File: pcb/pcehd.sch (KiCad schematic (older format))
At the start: 3 parts, among them U1 AP7361

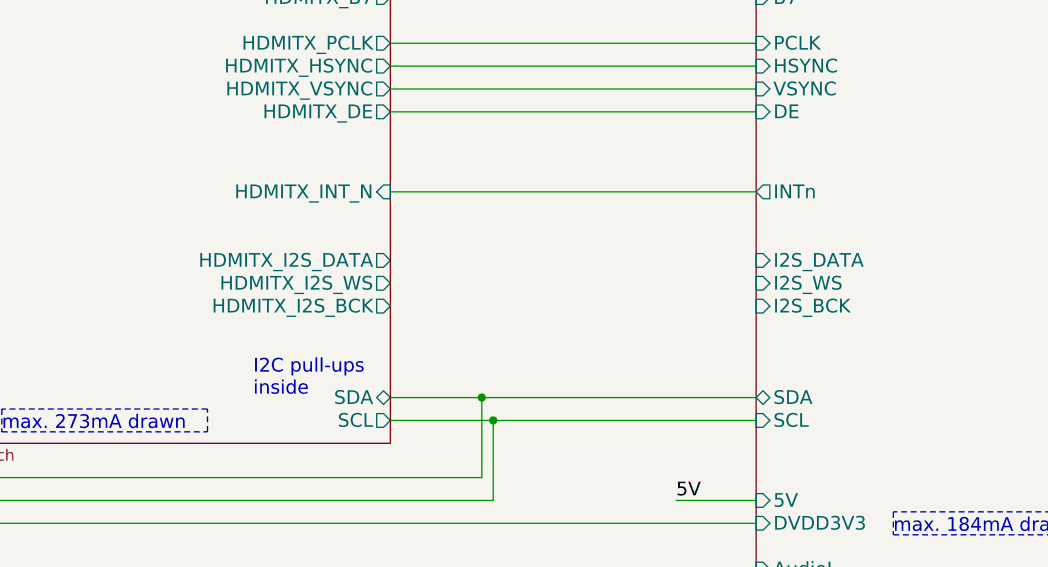
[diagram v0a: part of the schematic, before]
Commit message: Finished initial schematic with audio
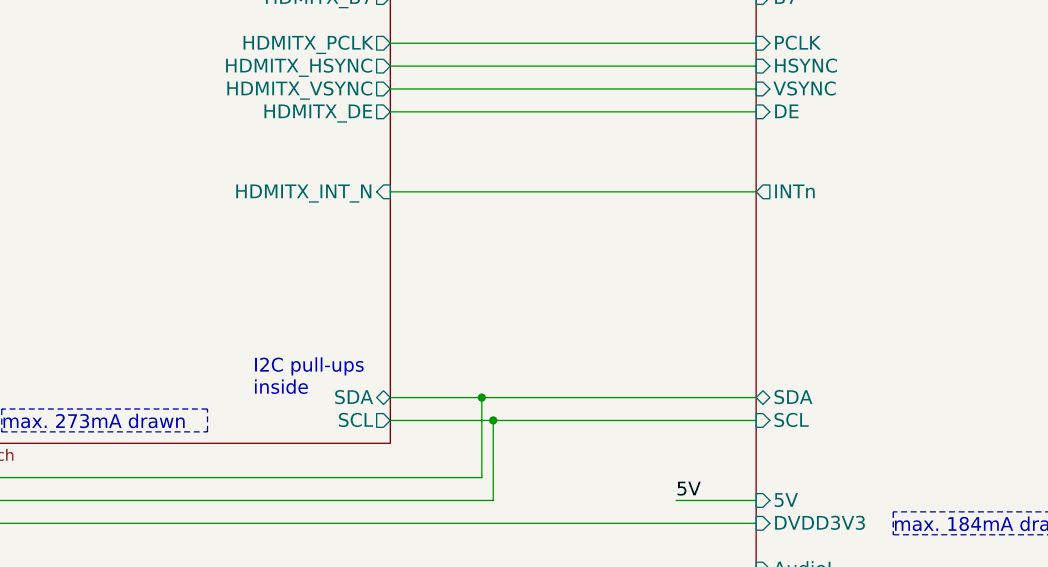
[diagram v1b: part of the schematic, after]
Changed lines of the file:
@@
 EESchema Schematic File Version 4
+LIBS:pcehd-cache
 EELAYER 30 0
 EELAYER END
@@
 F55 "DCK" I L 4650 4200 60
 F56 "CEK" I L 4650 4100 60
-F57 "HDMITX_I2S_DATA" O R 6750 4950 60
-F58 "HDMITX_I2S_WS" O R 6750 5050 60
-F59 "HDMITX_I2S_BCK" O R 6750 5150 60
-F60 "VD1" I L 4650 4750 60
-F61 "VD0" I L 4650 4650 60
-F62 "VD2" I L 4650 4850 60
-F63 "DDIR" O L 4650 2050 60
-F64 "A8" I L 4650 3000 60
-F65 "A9" I L 4650 3100 60
-F66 "A10" I L 4650 3200 60
-F67 "A11" I L 4650 3300 60
-F68 "A12" I L 4650 3400 60
-F69 "A16" I L 4650 3500 60
-F70 "A20" I L 4650 3600 60
-F71 "DCKSI" I L 4650 4300 60
-F72 "CDD" O L 4650 4400 60
-F73 "RST_N" O L 4650 4500 60
-F74 "SPBG" I L 4650 5450 60
-F75 "VD5" I L 4650 5150 60
-F76 "VD6" I L 4650 5250 60
-F77 "VD7" I L 4650 5350 60
+F57 "VD1" I L 4650 4750 60
+F58 "VD0" I L 4650 4650 60
+F59 "VD2" I L 4650 4850 60
+F60 "DDIR" O L 4650 2050 60
+F61 "A8" I L 4650 3000 60
+F62 "A9" I L 4650 3100 60
+F63 "A10" I L 4650 3200 60
+F64 "A11" I L 4650 3300 60
+F65 "A12" I L 4650 3400 60
+F66 "A16" I L 4650 3500 60
+F67 "A20" I L 4650 3600 60
+F68 "DCKSI" I L 4650 4300 60
+F69 "CDD" O L 4650 4400 60
+F70 "RST_N" O L 4650 4500 60
+F71 "SPBG" I L 4650 5450 60
+F72 "VD5" I L 4650 5150 60
+F73 "VD6" I L 4650 5250 60
+F74 "VD7" I L 4650 5350 60
 $EndSheet
 Wire Wire Line
@@
 F33 "DVDD3V3" I L 8350 6100 60
 F34 "5V" I L 8350 6000 60
-F35 "I2S_DATA" I L 8350 4950 60
-F36 "I2S_WS" I L 8350 5050 60
-F37 "I2S_BCK" I L 8350 5150 60
-F38 "AudioL" I L 8350 6300 60
-F39 "AudioR" I L 8350 6400 60
+F35 "AudioL" I L 8350 6300 60
+F36 "AudioR" I L 8350 6400 60
 $EndSheet
 $Sheet

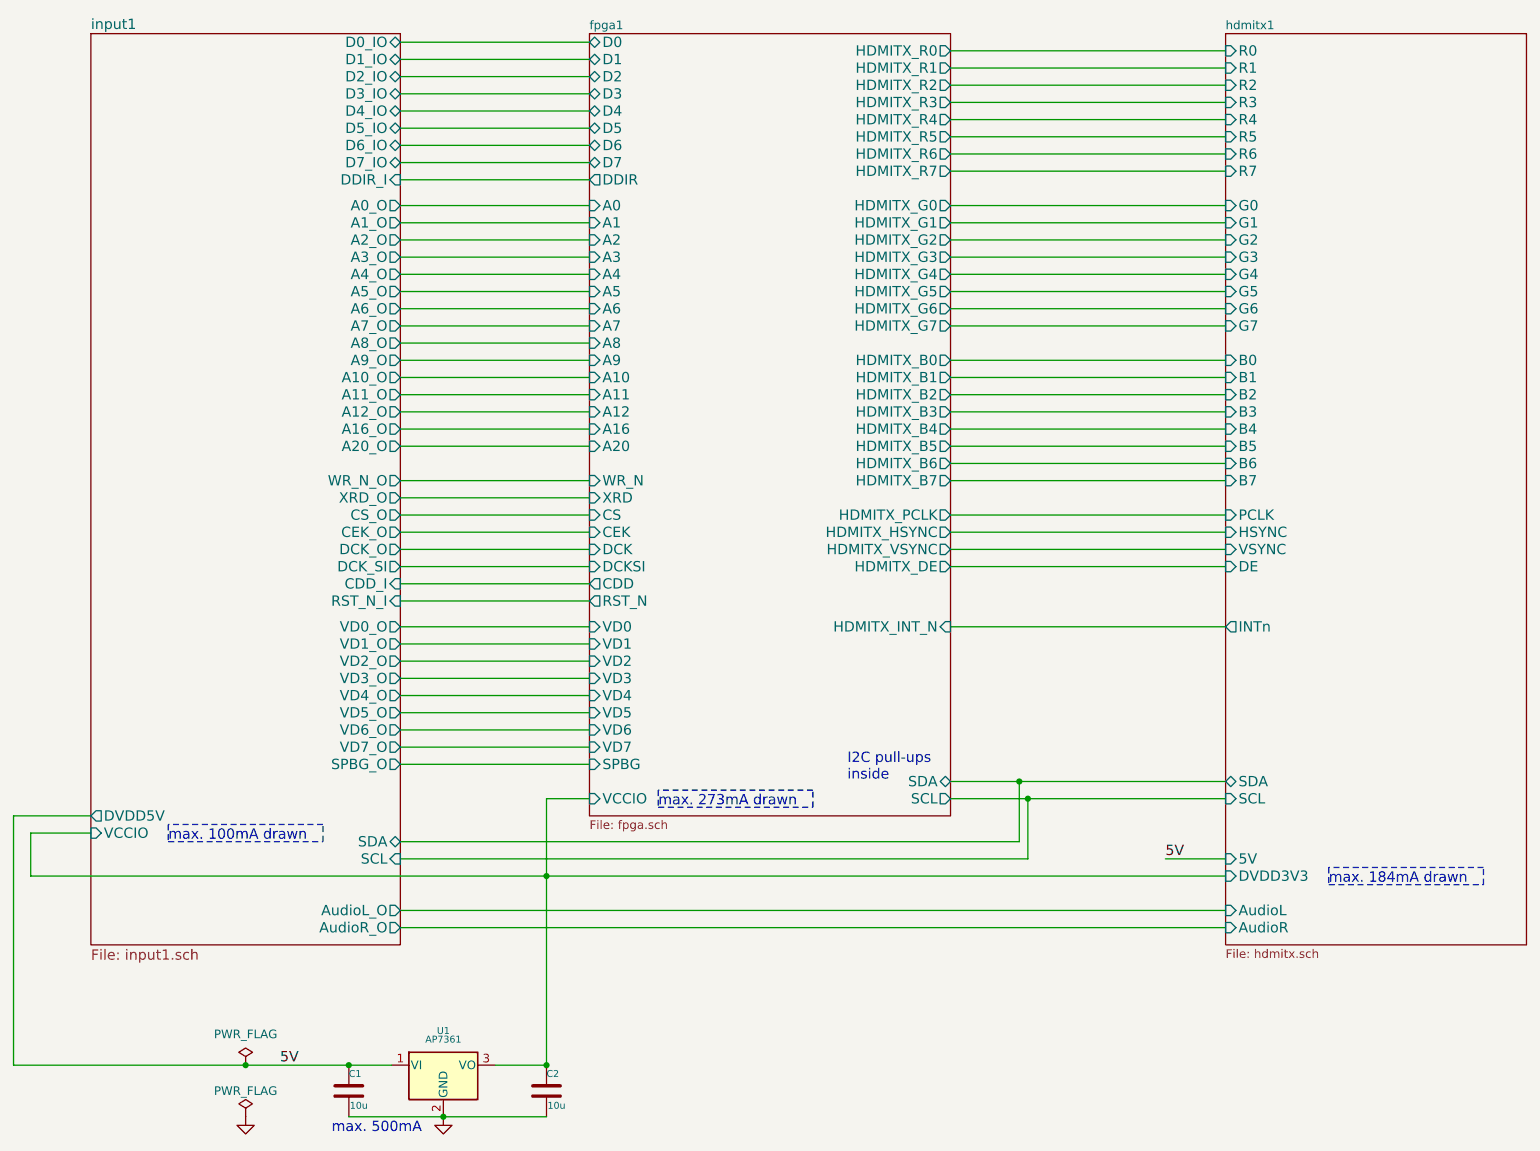
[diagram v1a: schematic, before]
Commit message: Cleaned up schematic, moved connections to busses
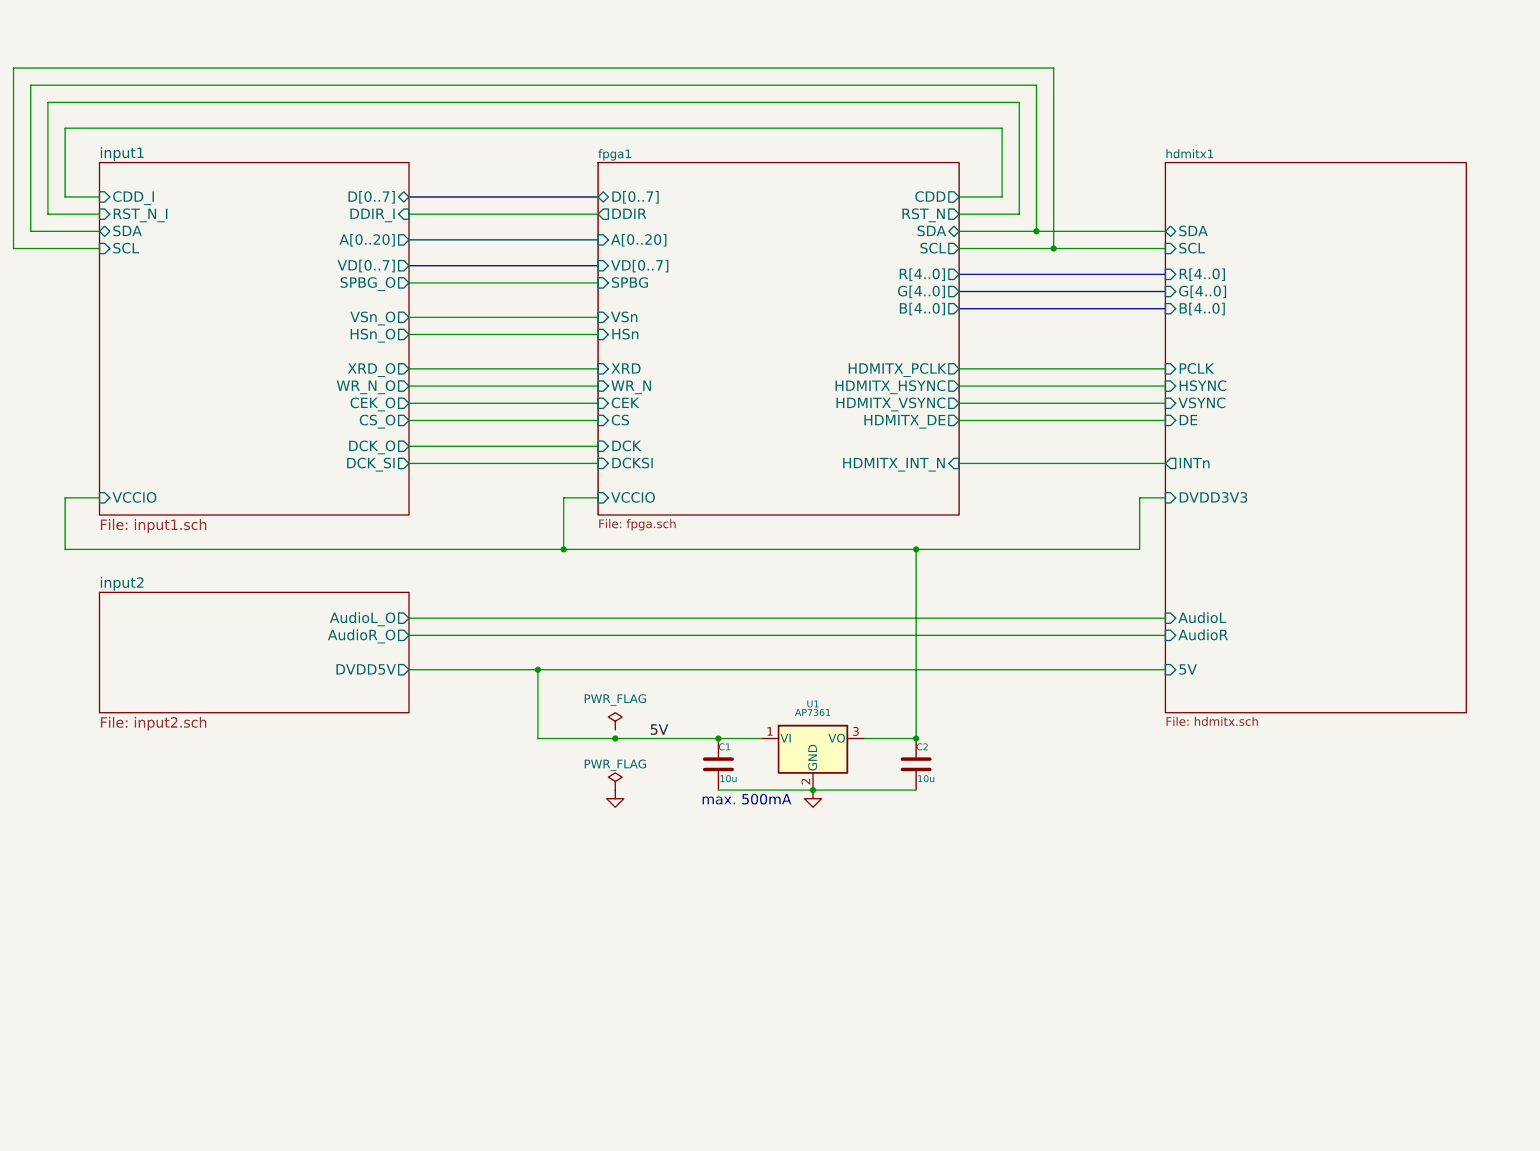
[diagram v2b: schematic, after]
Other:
- note removed: "I2C pull-ups\ninside"
- note removed: "max. 100mA drawn"
- note removed: "max. 184mA drawn"
- note removed: "max. 273mA drawn"
- moved on the sheet: C1, C2, U1

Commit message: Added clock selection
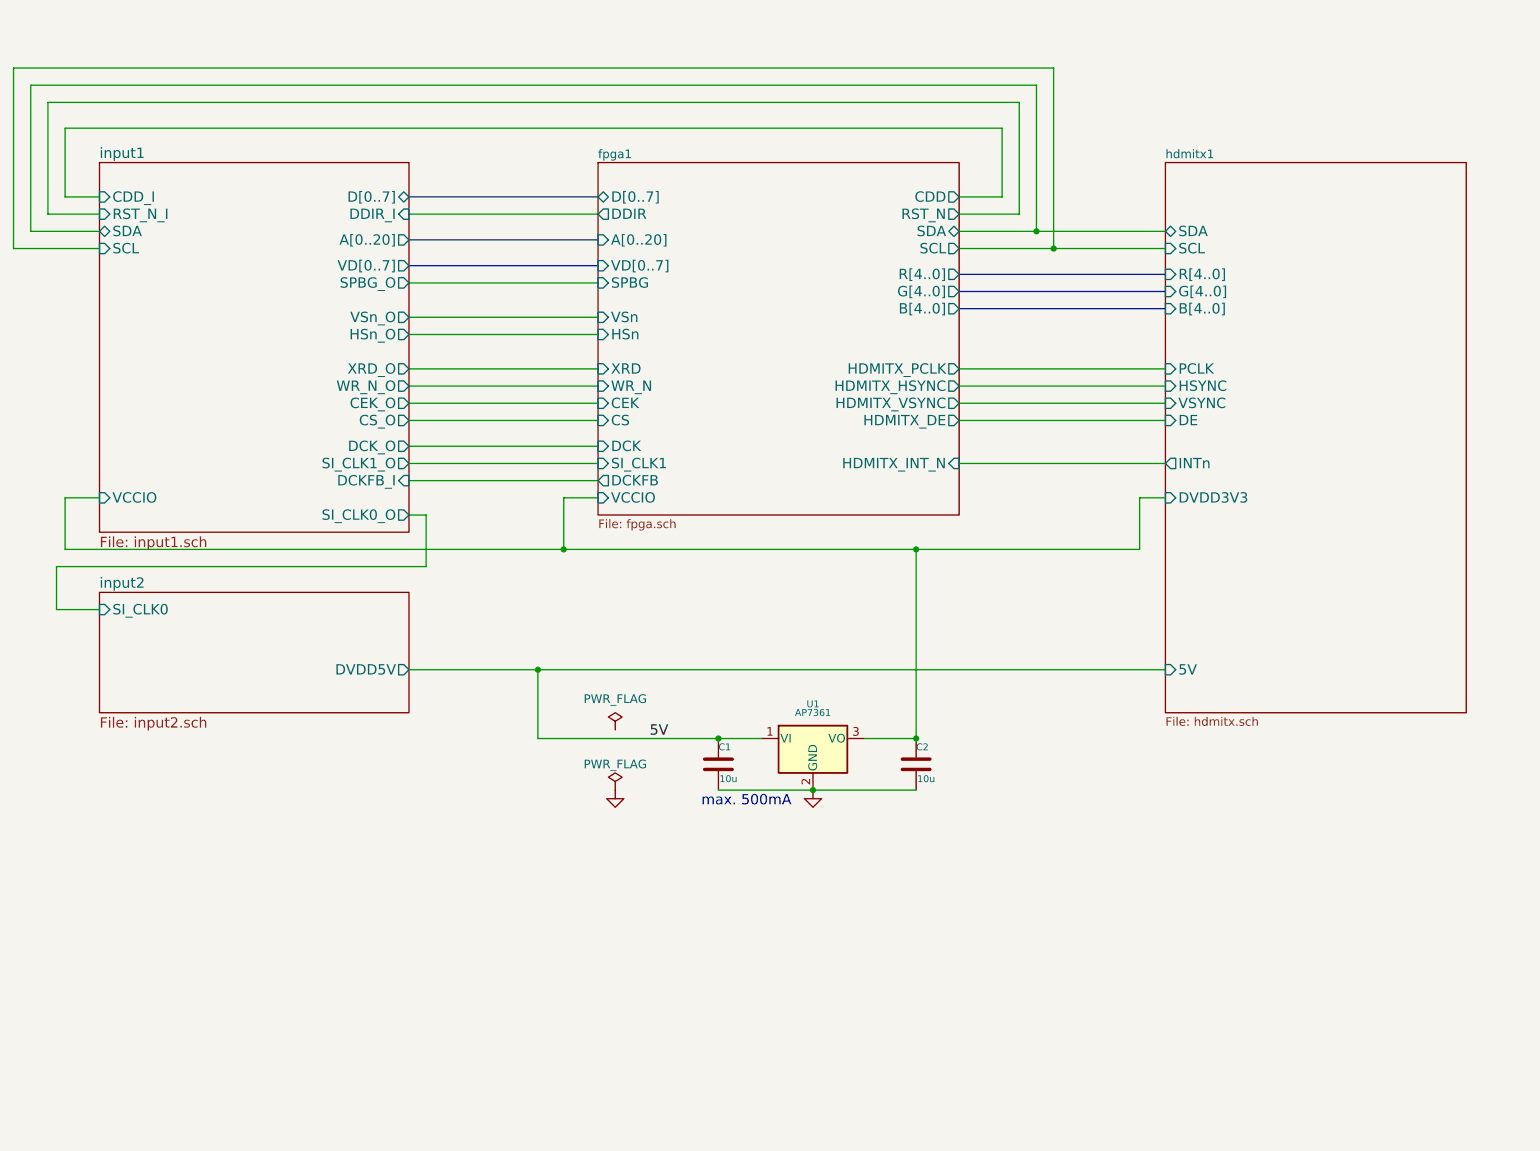
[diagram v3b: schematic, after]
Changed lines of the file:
@@
 EESchema Schematic File Version 4
+LIBS:pcehd-cache
 EELAYER 30 0
 EELAYER END
@@
 	1    0    0    -1
 $EndComp
-Wire Wire Line
-	4800 5300 5400 5300
 Connection ~ 5400 5300
 Connection ~ 5950 5600
@@
 F14 "CEK" I L 4700 3350 60
 F15 "DDIR" O L 4700 2250 60
-F16 "DCKSI" I L 4700 3700 60
-F17 "CDD" O R 6800 2150 60
-F18 "RST_N" O R 6800 2250 60
-F19 "SPBG" I L 4700 2650 60
-F20 "D[0..7]" B L 4700 2150 60
-F21 "A[0..20]" I L 4700 2400 60
-F22 "VD[0..7]" I L 4700 2550 60
-F23 "R[4..0]" O R 6800 2600 60
-F24 "G[4..0]" O R 6800 2700 60
-F25 "B[4..0]" O R 6800 2800 60
-F26 "VSn" I L 4700 2850 60
-F27 "HSn" I L 4700 2950 60
+F16 "CDD" O R 6800 2150 60
+F17 "RST_N" O R 6800 2250 60
+F18 "SPBG" I L 4700 2650 60
+F19 "D[0..7]" B L 4700 2150 60
+F20 "A[0..20]" I L 4700 2400 60
+F21 "VD[0..7]" I L 4700 2550 60
+F22 "R[4..0]" O R 6800 2600 60
+F23 "G[4..0]" O R 6800 2700 60
+F24 "B[4..0]" O R 6800 2800 60
+F25 "VSn" I L 4700 2850 60
+F26 "HSn" I L 4700 2950 60
+F27 "DCKFB" O L 4700 3800 60
+F28 "SI_CLK1" I L 4700 3700 60
 $EndSheet
 Wire Bus Line
@@
 	3600 3700 4700 3700
 $Sheet
-S 1800 1950 1800 2050
+S 1800 1950 1800 2150
 U 5A43CDD8
 F0 "input1" 60
@@
 F10 "CDD_I" I L 1800 2150 60
 F11 "DCK_O" O R 3600 3600 60
-F12 "DCK_SI" O R 3600 3700 60
-F13 "DDIR_I" I R 3600 2250 60
-F14 "SPBG_O" O R 3600 2650 60
-F15 "D[0..7]" B R 3600 2150 60
-F16 "A[0..20]" O R 3600 2400 60
-F17 "VSn_O" O R 3600 2850 60
-F18 "HSn_O" O R 3600 2950 60
-F19 "VD[0..7]" O R 3600 2550 60
+F12 "DDIR_I" I R 3600 2250 60
+F13 "SPBG_O" O R 3600 2650 60
+F14 "D[0..7]" B R 3600 2150 60
+F15 "A[0..20]" O R 3600 2400 60
+F16 "VSn_O" O R 3600 2850 60
+F17 "HSn_O" O R 3600 2950 60
+F18 "VD[0..7]" O R 3600 2550 60
+F19 "DCKFB_I" I R 3600 3800 60
+F20 "SI_CLK1_O" O R 3600 3700 60
+F21 "SI_CLK0_O" O R 3600 4000 60
 $EndSheet
 $Sheet
@@
 F0 "input2" 60
 F1 "input2.sch" 60
-F2 "AudioL_O" O R 3600 4600 60
-F3 "AudioR_O" O R 3600 4700 60
-F4 "DVDD5V" O R 3600 4900 60
+F2 "DVDD5V" O R 3600 4900 60
+F3 "SI_CLK0" I L 1800 4550 60
 $EndSheet
 Wire Wire Line
@@
 F9 "DVDD3V3" I L 8000 3900 60
 F10 "5V" I L 8000 4900 60
-F11 "AudioL" I L 8000 4600 60
-F12 "AudioR" I L 8000 4700 60
-F13 "R[4..0]" I L 8000 2600 60
-F14 "G[4..0]" I L 8000 2700 60
-F15 "B[4..0]" I L 8000 2800 60
+F11 "R[4..0]" I L 8000 2600 60
+F12 "G[4..0]" I L 8000 2700 60
+F13 "B[4..0]" I L 8000 2800 60
 $EndSheet
 Wire Wire Line
@@
 	6800 3700 8000 3700
 Wire Wire Line
-	3600 4600 8000 4600
-Wire Wire Line
-	3600 4700 8000 4700
-Wire Wire Line
 	3600 4900 4350 4900
 Wire Wire Line
-	4800 5300 4350 5300
-Wire Wire Line
 	4350 5300 4350 4900
-Connection ~ 4800 5300
 Connection ~ 4350 4900
 Wire Wire Line
@@
 	1600 3900 1600 4200
 Wire Wire Line
-	1600 4200 4500 4200
-Wire Wire Line
 	7850 4200 7850 3900
 Wire Wire Line
@@
 Wire Wire Line
 	4500 3900 4500 4200
-Connection ~ 4500 4200
 Wire Wire Line
 	4500 4200 6550 4200
@@
 Wire Wire Line
 	6550 4200 7850 4200
+Wire Wire Line
+	4350 5300 5400 5300
+Wire Wire Line
+	3600 3800 4700 3800
+Connection ~ 4500 4200
+Wire Wire Line
+	1600 4200 4500 4200
+Wire Wire Line
+	3600 4000 3700 4000
+Wire Wire Line
+	3700 4000 3700 4300
+Wire Wire Line
+	3700 4300 1550 4300
+Wire Wire Line
+	1550 4300 1550 4550
+Wire Wire Line
+	1550 4550 1800 4550
 $EndSCHEMATC

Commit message: Added FS7140 PLL, moved to level-shift '245
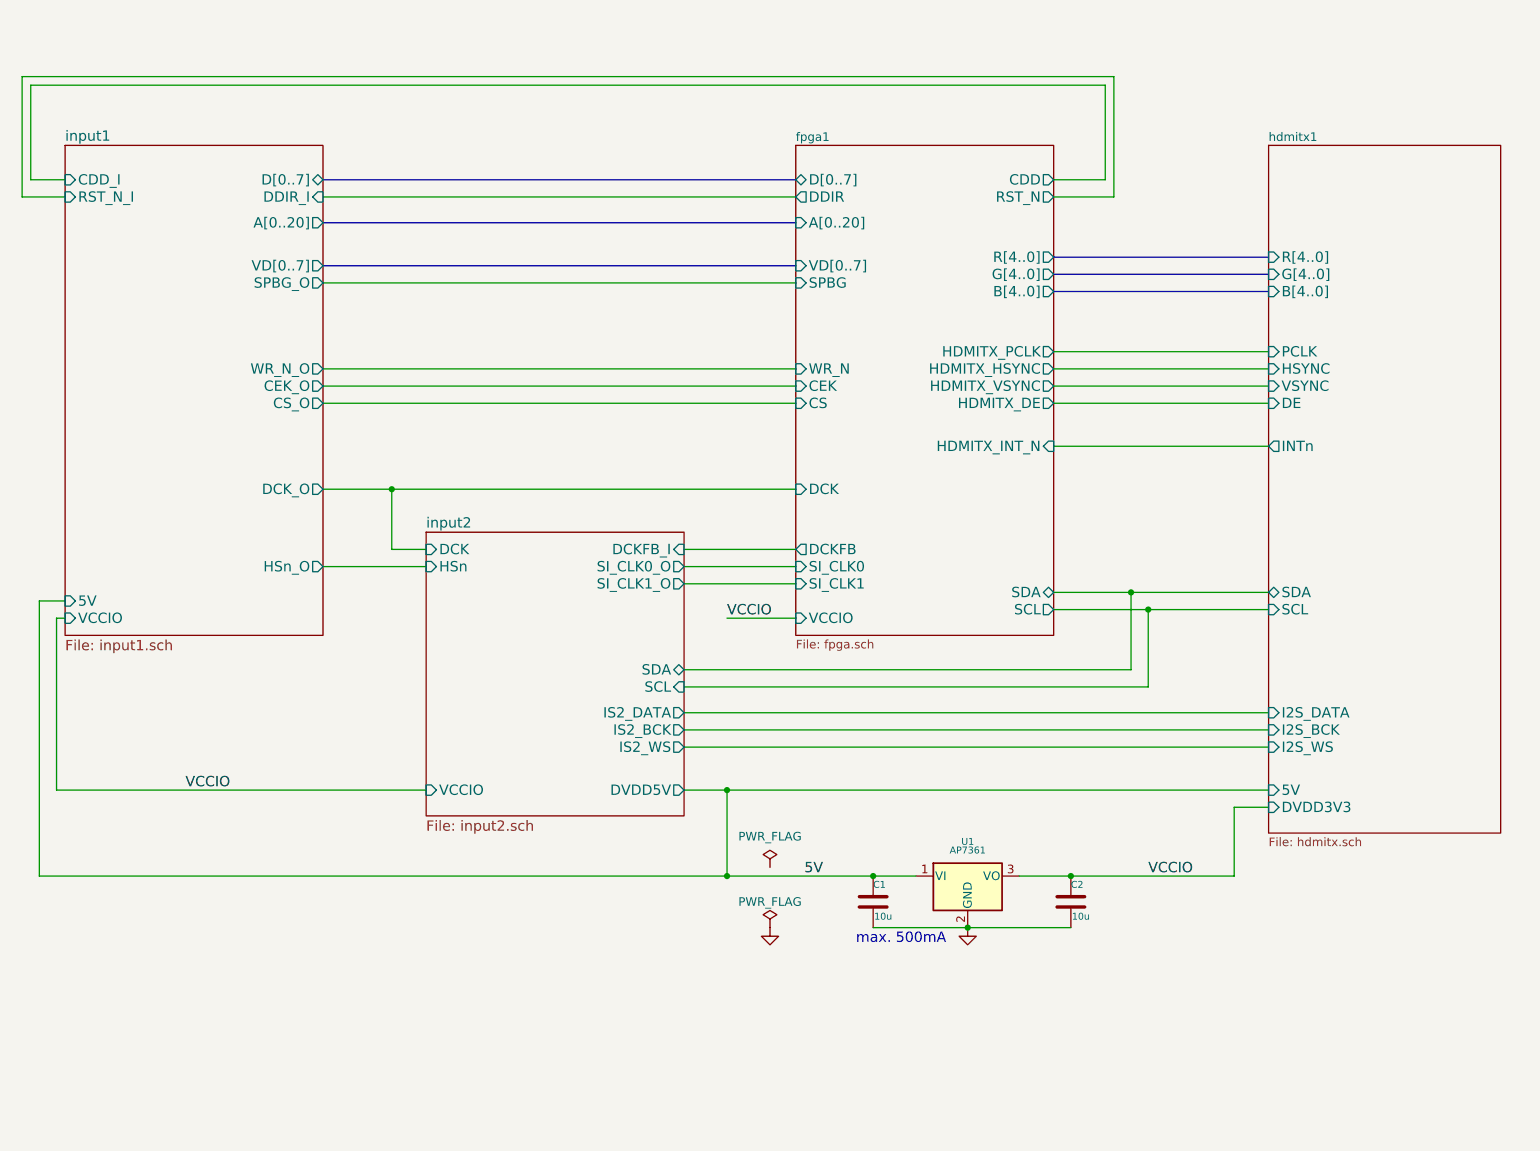
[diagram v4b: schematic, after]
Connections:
- net fpga1/VCCIO renamed VCCIO
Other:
- moved on the sheet: C1, C2, U1
